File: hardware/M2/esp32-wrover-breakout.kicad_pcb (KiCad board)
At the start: 2 copper layers, 25.4 x 32 mm, 10 parts, among them IC1 ESP32-WROVER-E_M213EH6464PH3Q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, J1 Conn_01x06_Male, J2 Conn_01x10_Male, J3 Conn_01x10_Male, Q1 MUN5214DW1T1G, U1 XC6220B331MR

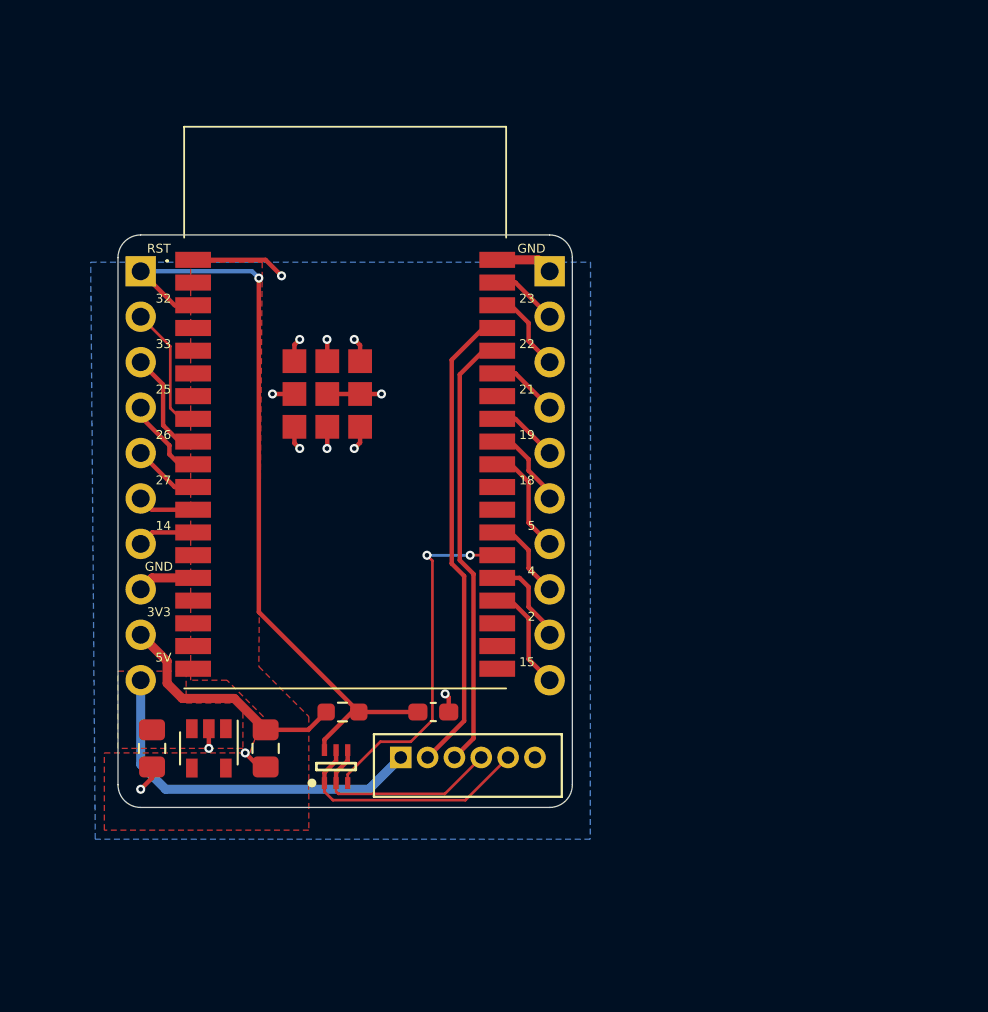
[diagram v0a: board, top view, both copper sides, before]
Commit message: M.2 schematic + first placement
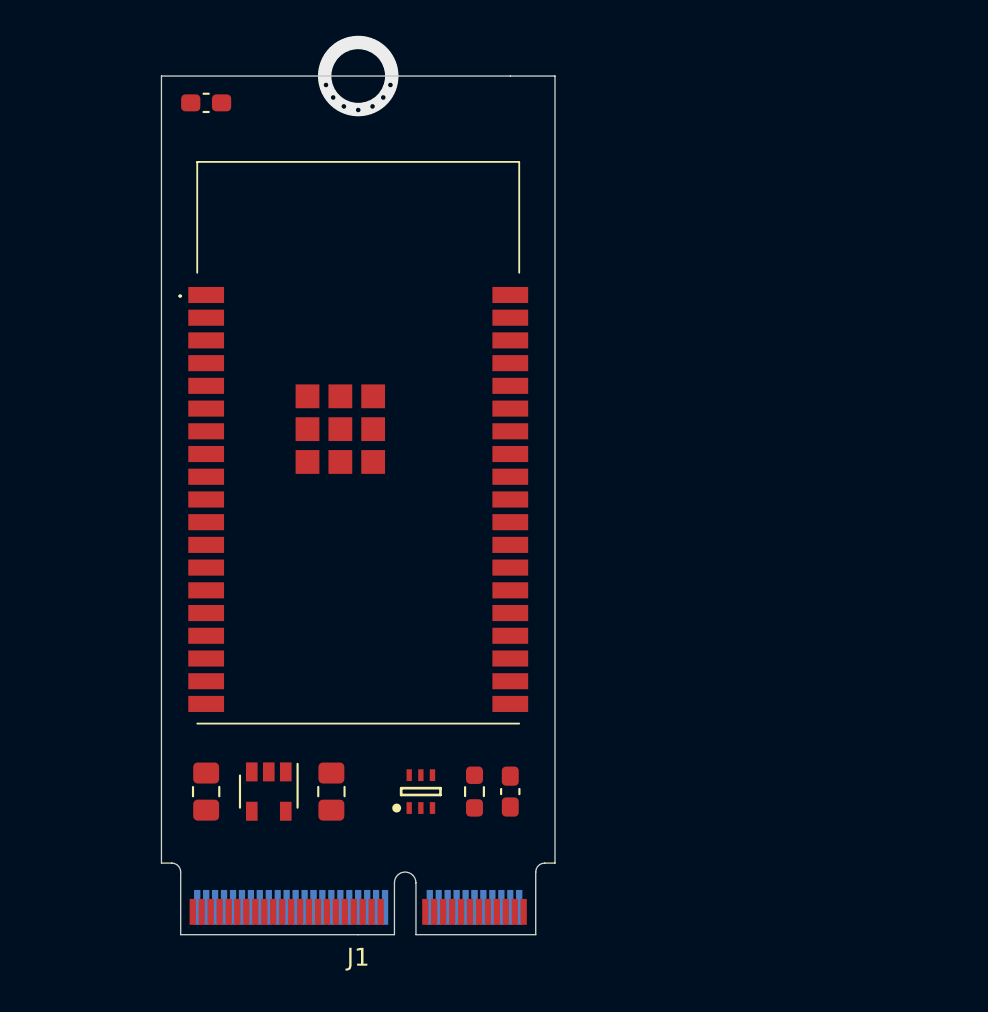
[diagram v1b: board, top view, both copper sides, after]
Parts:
- removed J2, J3: Conn_01x10_Male, Connector_PinHeader_2.54mm:PinHeader_1x10_P2.54mm_Vertical
- added C2: 0.1uF, Capacitor_SMD:C_0603_1608Metric_Pad1.08x0.95mm_HandSolder, F.Cu at (42.3, 26.4)
- J1: value Conn_01x06_Male -> Edge_Conn_NGFF_E_Key; footprint B6B-ZR(LF)(SN):JST_B6B-ZR(LF)(SN) -> NGFF:NGFF_E
- moved J1 11.6 mm to (50.8, 72.9), turned to 0 degrees
- moved R1 8.62 mm to (57.3, 64.9), turned to 90 degrees
- moved C3 6.19 mm to (59.3, 64.9), turned to 270 degrees
- moved Q1 4.94 mm to (54.3, 64.9)
- moved C4 4.40 mm to (49.3, 64.9)
- moved U1 4.13 mm to (45.8, 64.9)
- moved C1 3.87 mm to (42.3, 64.9)
- moved IC1 2.10 mm to (50.8, 45.4)
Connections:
- IC1 pad 10: /GPIO25 -> /GPIO25-DAC1
- IC1 pad 11: /GPIO26 -> /GPIO26-DAC2
- IC1 pad 14: Net-(IC1-Pad14) -> /GPIO12
- IC1 pad 27: Net-(IC1-Pad27) -> /GPIO16
- IC1 pad 29: /GPIO5 -> /GPIO5-CS
- IC1 pad 30: /GPIO18 -> /GPIO18-SCK
- IC1 pad 31: /GPIO19 -> /GPIO19-MISO
- IC1 pad 33: /GPIO21 -> /GPIO21-SDA
- IC1 pad 36: /GPIO22 -> /GPIO22-SCL
- IC1 pad 37: /GPIO23 -> /GPIO23-MOSI
- J1 pad 1: +5V -> GND
- J1 pad 2: /TX -> +3V3
- J1 pad 3: /RX -> Net-(J1-Pad3)
- J1 pad 4: /DTR -> +3V3
- J1 pad 5: /RTS -> Net-(J1-Pad5)
- J1 pad 6: GND -> /RESET
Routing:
- net /RESET: track 43.5 -> 0.00 mm, vias 1 -> 0
- net GND: track 29.0 -> 0.00 mm, vias 13 -> 0
- net /TX: track 26.6 -> 0.00 mm
- net /RX: track 24.8 -> 0.00 mm
- net +5V: track 20.6 -> 0.00 mm
- net /GPIO0: track 19.7 -> 0.00 mm, vias 2 -> 0
- net /RTS: track 14.0 -> 0.00 mm
- net +3V3: track 13.7 -> 0.00 mm
- net /DTR: track 11.6 -> 0.00 mm
- net /GPIO32: track 7.32 -> 0.00 mm
- net /GPIO5: track 6.11 -> 0.00 mm
- net /GPIO15: track 6.11 -> 0.00 mm
- net /GPIO33: track 6.10 -> 0.00 mm
- net /GPIO2: track 5.13 -> 0.00 mm
- net /GPIO4: track 4.84 -> 0.00 mm
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- removed copper zone on F.Cu, net +3V3
- removed copper zone on F.Cu, net +5V
- removed copper zone on B.Cu, net GND
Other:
- board size 25.4 x 32 mm -> 22 x 44 mm
- board text added: "François Gervais 12 jan 2021 rev 2.0"
- board text added: "NO COMPONENTS"
- board text removed: "14"
- board text removed: "15"
- board text removed: "18"
- board text removed: "19"
- board text removed: "2"
- board text removed: "21"
- board text removed: "22"
- board text removed: "23"
- board text removed: "25"
- board text removed: "26"
- board text removed: "27"
- board text removed: "32"
- board text removed: "33"
- board text removed: "3V3"
- board text removed: "4"
- board text removed: "5"
- board text removed: "5V"
- board text removed: "François Gervais 29 dec 2020 rev 1.0"
- board text removed: "GND"
- board text removed: "RST"

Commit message: First M.2 routing
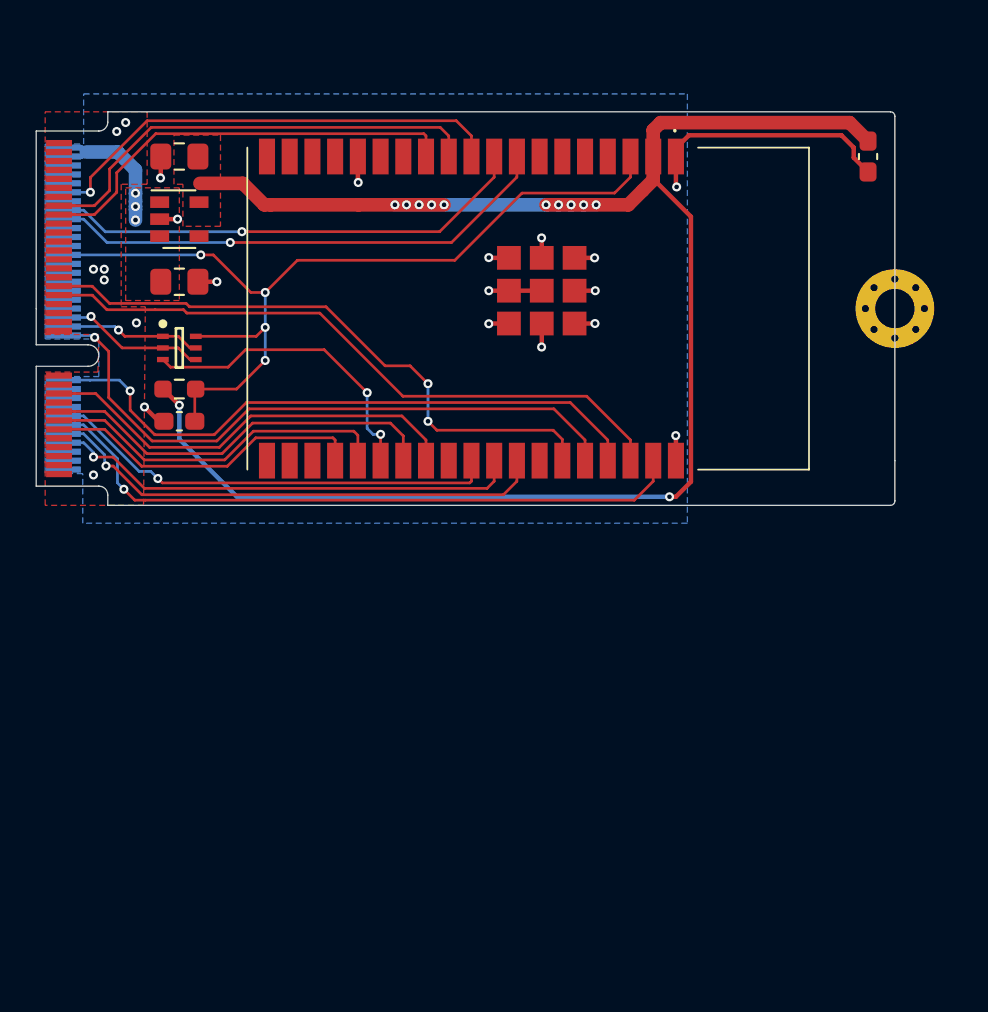
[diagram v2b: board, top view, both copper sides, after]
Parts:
- added REF**: MountingHole_2.2mm_M2_Pad_Via, MountingHole:MountingHole_2.2mm_M2_Pad_Via, F.Cu at (80.8, 37.9)
- moved J1 39.4 mm to (32.8, 37.9), turned to 270 degrees
- moved C2 37.1 mm to (79.3, 29.4), turned to 270 degrees
- moved C4 36.5 mm to (40.8, 29.4), turned to 180 degrees
- moved U1 32.4 mm to (40.8, 32.9), turned to 0 degrees
- moved C1 28.5 mm to (40.8, 36.4), turned to 0 degrees
- moved Q1 28.2 mm to (40.8, 40.1), turned to 0 degrees
- moved R1 27.9 mm to (40.8, 42.4), turned to 0 degrees
- moved C3 27.8 mm to (40.8, 44.2), turned to 180 degrees
- moved IC1 12.1 mm to (60.3, 37.9), turned to 270 degrees
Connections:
- net Net-(IC1-Pad6) renamed /GPIO34
- IC1 pad 29: /GPIO5-CS -> /GPIO5
- IC1 pad 30: /GPIO18-SCK -> /GPIO18
- IC1 pad 31: /GPIO19-MISO -> /GPIO19
- IC1 pad 33: /GPIO21-SDA -> /GPIO21
- IC1 pad 36: /GPIO22-SCL -> /GPIO22
- IC1 pad 37: /GPIO23-MOSI -> /GPIO23
- J1 pad 10: /GPIO26-DAC2 -> /GPIO19
- J1 pad 12: /GPIO27 -> /GPIO23
- J1 pad 14: Net-(J1-Pad14) -> /GPIO5
- J1 pad 17: /GPIO12 -> Net-(J1-Pad17)
- J1 pad 2: +3V3 -> Net-(J1-Pad2)
- J1 pad 35: /GPIO18-SCK -> Net-(J1-Pad35)
- J1 pad 37: /GPIO19-MISO -> Net-(J1-Pad37)
- J1 pad 38: +5V -> Net-(J1-Pad38)
- J1 pad 4: +3V3 -> Net-(J1-Pad4)
- J1 pad 40: /GPIO32 -> Net-(J1-Pad40)
- J1 pad 41: /GPIO23-MOSI -> /GPIO22
- J1 pad 42: /GPIO33 -> Net-(J1-Pad42)
- J1 pad 43: /GPIO5-CS -> /GPIO21
- J1 pad 50: Net-(J1-Pad50) -> /RESET
- J1 pad 58: /GPIO21-SDA -> /GPIO32
- J1 pad 59: Net-(J1-Pad59) -> /GPIO27
- J1 pad 6: /RESET -> Net-(J1-Pad6)
- J1 pad 60: /GPIO22-SCL -> /GPIO33
- J1 pad 61: Net-(J1-Pad61) -> /GPIO26-DAC2
- J1 pad 64: Net-(J1-Pad64) -> /GPIO25-DAC1
- J1 pad 72: +3V3 -> +5V
- J1 pad 74: +3V3 -> +5V
- J1 pad 8: /GPIO25-DAC1 -> /GPIO18
- J1 pad 9: /GPIO14 -> Net-(J1-Pad9)
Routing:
- net +3V3: track 0.00 -> 99.9 mm, vias 0 -> 12
- net /RESET: track 0.00 -> 50.6 mm, vias 0 -> 4
- net /GPIO23: track 0.00 -> 37.1 mm, vias 0 -> 1
- net /GPIO22: track 0.00 -> 36.5 mm
- net /RX: track 0.00 -> 35.7 mm, vias 0 -> 1
- net /TX: track 0.00 -> 35.1 mm, vias 0 -> 1
- net /GPIO21: track 0.00 -> 34.1 mm, vias 0 -> 2
- net GND: track 0.00 -> 33.0 mm, vias 0 -> 22
- net /GPIO32: track 0.00 -> 28.6 mm, vias 0 -> 1
- net /GPIO19: track 0.00 -> 28.5 mm, vias 0 -> 1
- net /GPIO33: track 0.00 -> 27.0 mm, vias 0 -> 1
- net /GPIO18: track 0.00 -> 26.6 mm, vias 0 -> 1
- net /GPIO26-DAC2: track 0.00 -> 26.5 mm
- net /GPIO25-DAC1: track 0.00 -> 26.4 mm, vias 0 -> 1
- net /GPIO5: track 0.00 -> 25.5 mm, vias 0 -> 1
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- added copper zone on F.Cu, net +3V3
- added copper zone on F.Cu, net +5V
- added copper zone on B.Cu, net GND
- added copper zone on F.Cu, net GND
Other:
- board size 22 x 44 mm -> 44 x 22 mm
- net class Default: clearance 0.2 -> 0.1524
- rule trace_clearance: 0.2 -> 0.1524

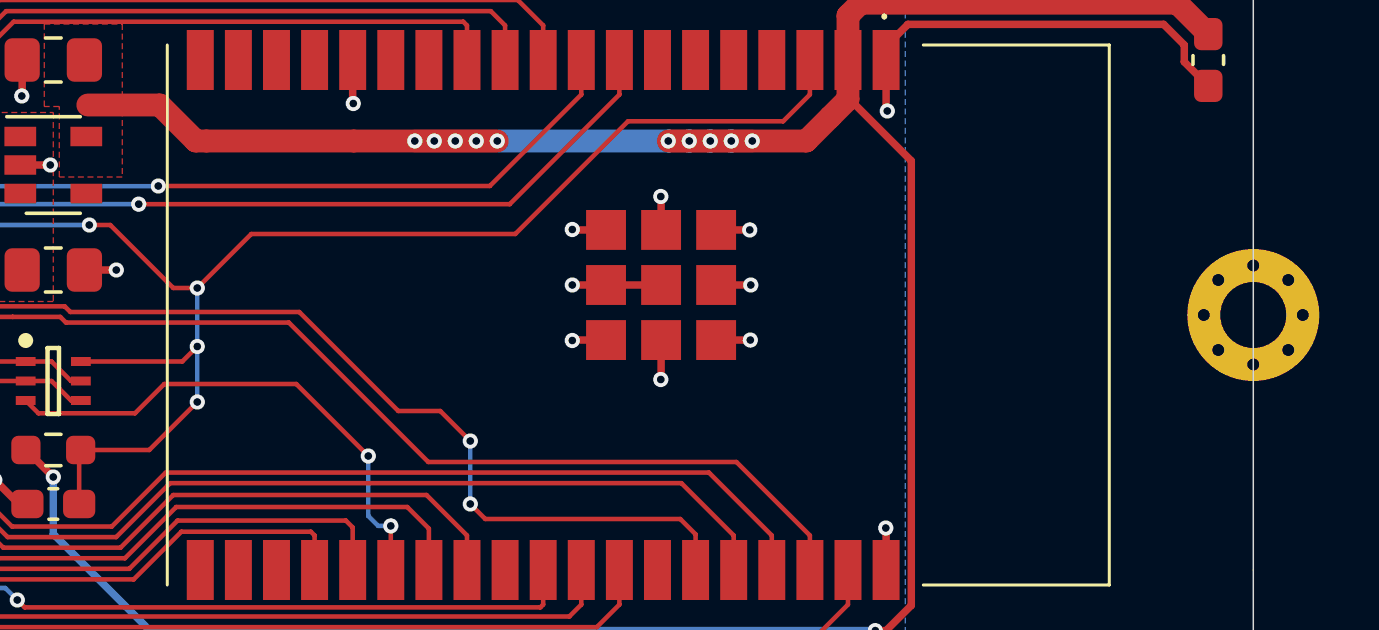
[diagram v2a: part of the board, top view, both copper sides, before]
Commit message: Rotate the screw pad
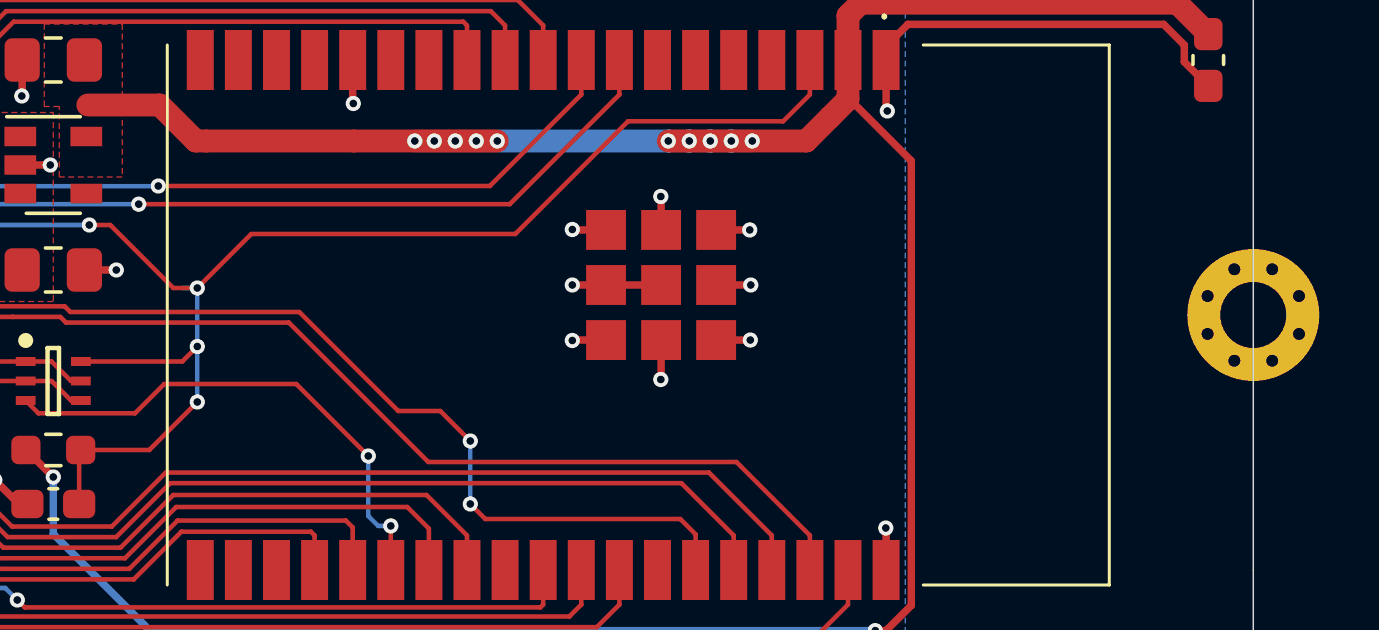
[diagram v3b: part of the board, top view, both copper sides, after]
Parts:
- turned REF** to 22.5 degrees
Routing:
- net /RESET: track 50.6 -> 51.1 mm
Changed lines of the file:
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@@
     (thickness 1.6)
     (drawings 10)
-    (tracks 320)
+    (tracks 321)
     (zones 0)
     (modules 10)
@@
   )
   (module MountingHole:MountingHole_2.2mm_M2_Pad_Via (layer F.Cu)
-    (at 80.768 37.899)
+    (at 80.768 37.899 22.5)
     (descr "Mounting Hole 2.2mm, M2")
     (tags "mounting hole 2.2mm m2")
     (attr virtual)
-    (fp_text reference REF** (at 0 -3.2) (layer F.SilkS) hide
-      (effects (font (size 1 1) (thickness 0.15)))
-    )
-    (fp_text value MountingHole_2.2mm_M2_Pad_Via (at 0 3.2) (layer F.Fab)
-      (effects (font (size 1 1) (thickness 0.15)))
-    )
-    (fp_text user %R (at 0.3 0) (layer F.Fab)
+    (fp_text reference REF** (at 0 -3.2 22.5) (layer F.SilkS) hide
+      (effects (font (size 1 1) (thickness 0.15)))
+    )
+    (fp_text value MountingHole_2.2mm_M2_Pad_Via (at 0 3.2 22.5) (layer F.Fab)
+      (effects (font (size 1 1) (thickness 0.15)))
+    )
+    (fp_text user %R (at 0.3 0 22.5) (layer F.Fab)
       (effects (font (size 1 1) (thickness 0.15)))
     )
     (fp_circle (center 0 0) (end 2.2 0) (layer Cmts.User) (width 0.15))
     (fp_circle (center 0 0) (end 2.45 0) (layer F.CrtYd) (width 0.05))
-    (pad 1 thru_hole circle (at 1.166726 -1.166726) (size 0.7 0.7) (drill 0.4) (layers *.Cu *.Mask))
-    (pad 1 thru_hole circle (at 0 -1.65) (size 0.7 0.7) (drill 0.4) (layers *.Cu *.Mask))
-    (pad 1 thru_hole circle (at -1.166726 -1.166726) (size 0.7 0.7) (drill 0.4) (layers *.Cu *.Mask))
-    (pad 1 thru_hole circle (at -1.65 0) (size 0.7 0.7) (drill 0.4) (layers *.Cu *.Mask))
-    (pad 1 thru_hole circle (at -1.166726 1.166726) (size 0.7 0.7) (drill 0.4) (layers *.Cu *.Mask))
-    (pad 1 thru_hole circle (at 0 1.65) (size 0.7 0.7) (drill 0.4) (layers *.Cu *.Mask))
-    (pad 1 thru_hole circle (at 1.166726 1.166726) (size 0.7 0.7) (drill 0.4) (layers *.Cu *.Mask))
-    (pad 1 thru_hole circle (at 1.65 0) (size 0.7 0.7) (drill 0.4) (layers *.Cu *.Mask))
-    (pad 1 thru_hole circle (at 0 0) (size 4.4 4.4) (drill 2.2) (layers *.Cu *.Mask))
+    (pad 1 thru_hole circle (at 1.166726 -1.166726 22.5) (size 0.7 0.7) (drill 0.4) (layers *.Cu *.Mask))
+    (pad 1 thru_hole circle (at 0 -1.65 22.5) (size 0.7 0.7) (drill 0.4) (layers *.Cu *.Mask))
+    (pad 1 thru_hole circle (at -1.166726 -1.166726 22.5) (size 0.7 0.7) (drill 0.4) (layers *.Cu *.Mask))
+    (pad 1 thru_hole circle (at -1.65 0 22.5) (size 0.7 0.7) (drill 0.4) (layers *.Cu *.Mask))
+    (pad 1 thru_hole circle (at -1.166726 1.166726 22.5) (size 0.7 0.7) (drill 0.4) (layers *.Cu *.Mask))
+    (pad 1 thru_hole circle (at 0 1.65 22.5) (size 0.7 0.7) (drill 0.4) (layers *.Cu *.Mask))
+    (pad 1 thru_hole circle (at 1.166726 1.166726 22.5) (size 0.7 0.7) (drill 0.4) (layers *.Cu *.Mask))
+    (pad 1 thru_hole circle (at 1.65 0 22.5) (size 0.7 0.7) (drill 0.4) (layers *.Cu *.Mask))
+    (pad 1 thru_hole circle (at 0 0 22.5) (size 4.4 4.4) (drill 2.2) (layers *.Cu *.Mask))
   )
   (module MUN5214DW1T1G:On_Semiconductor-MUN5214DW1T1G-Manufacturer_Recommended (layer F.Cu)
@@
   (segment (start 35.318 28.899) (end 35.568 29.149) (width 0.25) (layer B.Cu) (net 2))
   (segment (start 35.568 29.149) (end 37.318 29.149) (width 0.762) (layer B.Cu) (net 2))
+  (segment (start 45.068 36.999) (end 45.568 36.999) (width 0.1524) (layer B.Cu) (net 4))
   (zone (net 2) (net_name +5V) (layer F.Cu) (hatch edge 0.508)
     (connect_pads (clearance 0.1524))

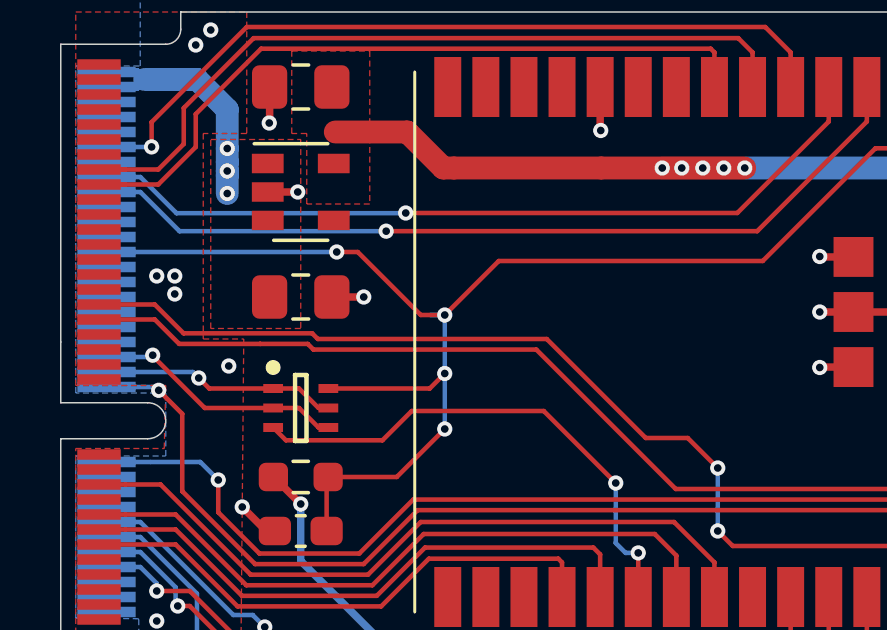
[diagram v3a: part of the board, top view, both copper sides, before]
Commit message: Remove a little piece of track
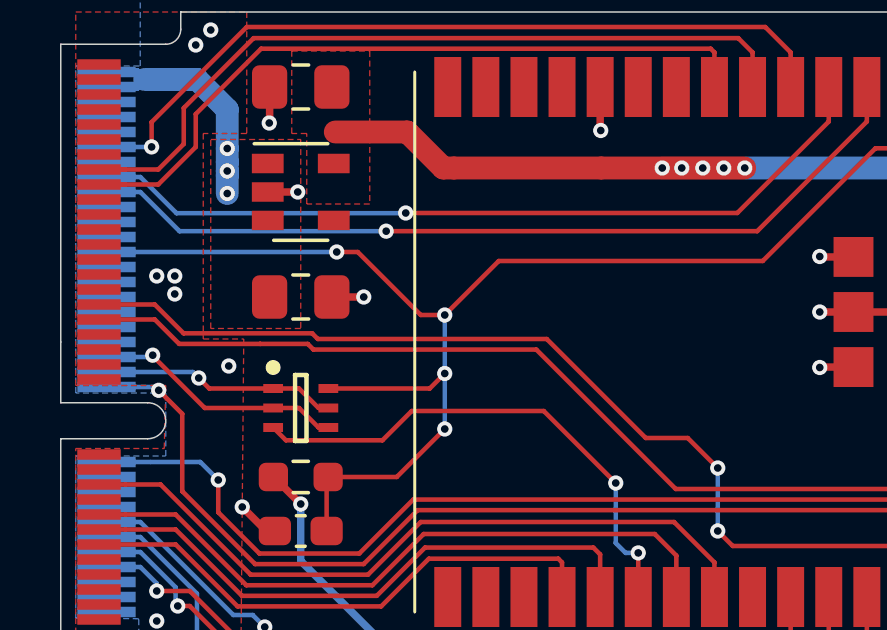
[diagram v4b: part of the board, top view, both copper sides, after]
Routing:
- net /RESET: track 51.1 -> 50.6 mm
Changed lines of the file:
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@@
     (thickness 1.6)
     (drawings 10)
-    (tracks 321)
+    (tracks 320)
     (zones 0)
     (modules 10)
@@
   (segment (start 35.318 28.899) (end 35.568 29.149) (width 0.25) (layer B.Cu) (net 2))
   (segment (start 35.568 29.149) (end 37.318 29.149) (width 0.762) (layer B.Cu) (net 2))
-  (segment (start 45.068 36.999) (end 45.568 36.999) (width 0.1524) (layer B.Cu) (net 4))
   (zone (net 2) (net_name +5V) (layer F.Cu) (hatch edge 0.508)
     (connect_pads (clearance 0.1524))
